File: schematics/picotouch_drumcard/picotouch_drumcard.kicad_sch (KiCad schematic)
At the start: 77 parts, among them J1 AudioJack4, J2 AudioJack4, J3 AudioJack4, SW1 Capacitive Button, SW10 Capacitive Button, SW11 Capacitive Button, SW12 Capacitive Button, SW13 Capacitive Button, SW14 Capacitive Button, SW15 Capacitive Button, SW16 Capacitive Button, SW17 Capacitive Button, SW2 Capacitive Button, SW3 Capacitive Button, SW4 Capacitive Button, SW5 Capacitive Button, SW6 Capacitive Button, SW7 Capacitive Button, SW8 Capacitive Button, SW9 Capacitive Button, U1 Pico, U2 H11L1S(TA), U3 MCP73831-2-OT, U4 TS20, X1 AFC20-S02ACA-00

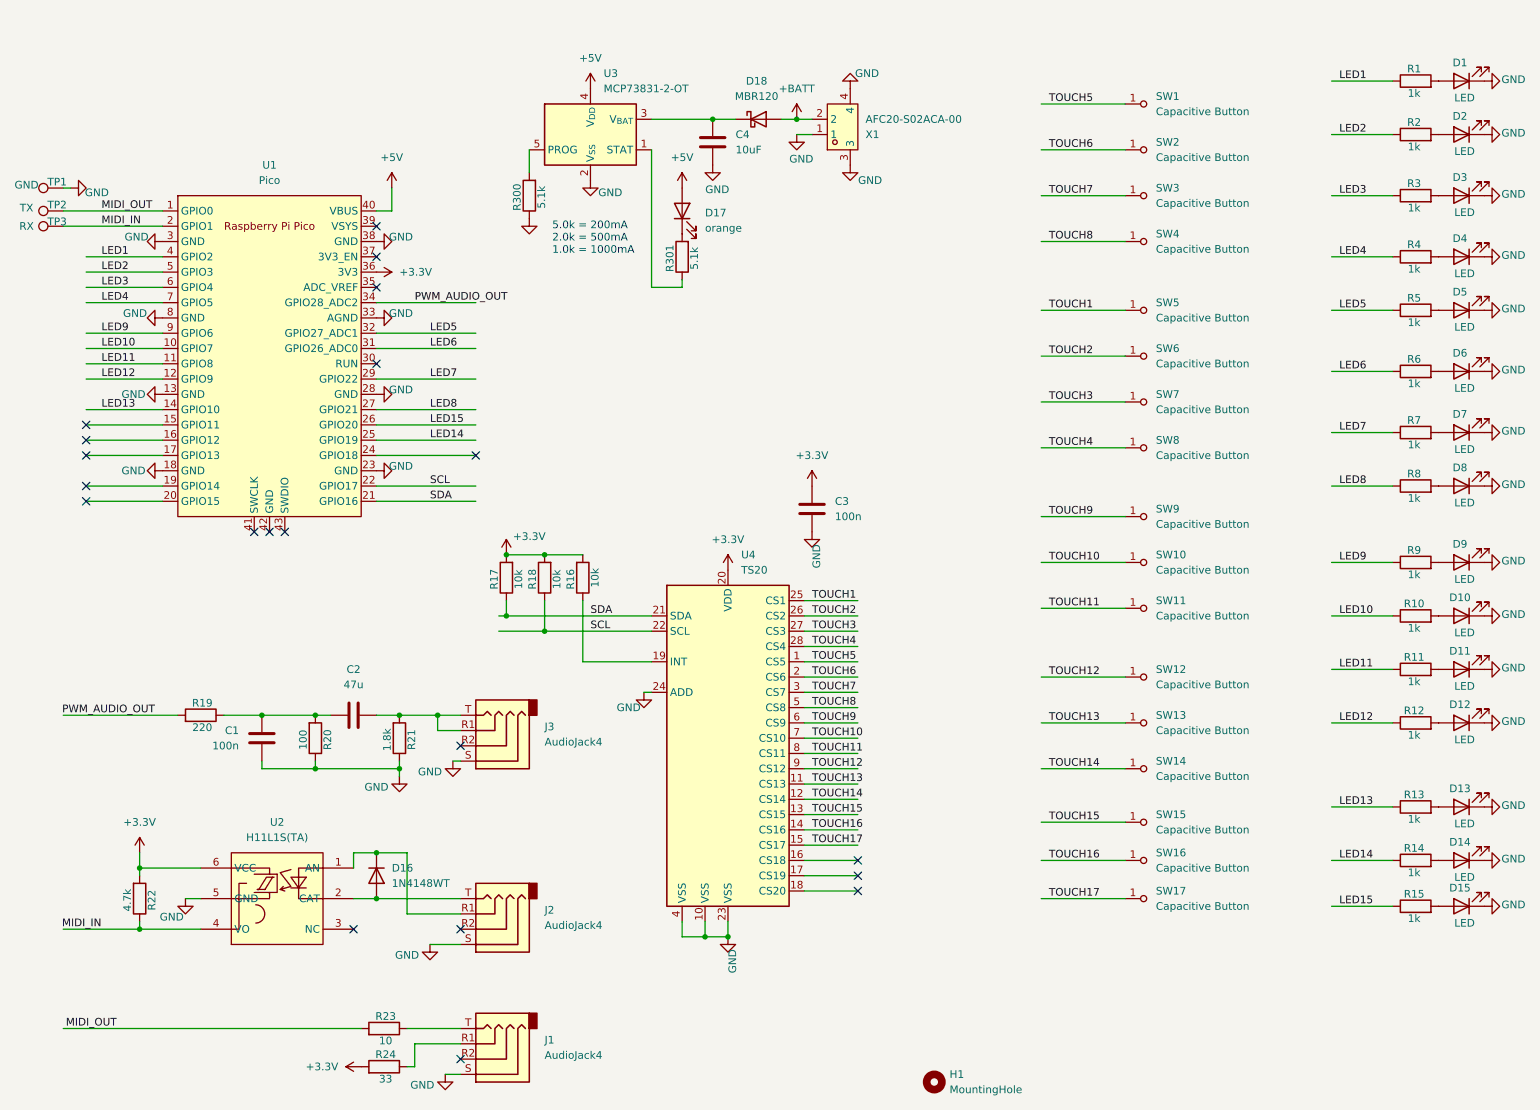
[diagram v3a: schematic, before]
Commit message: add missing cap on opto
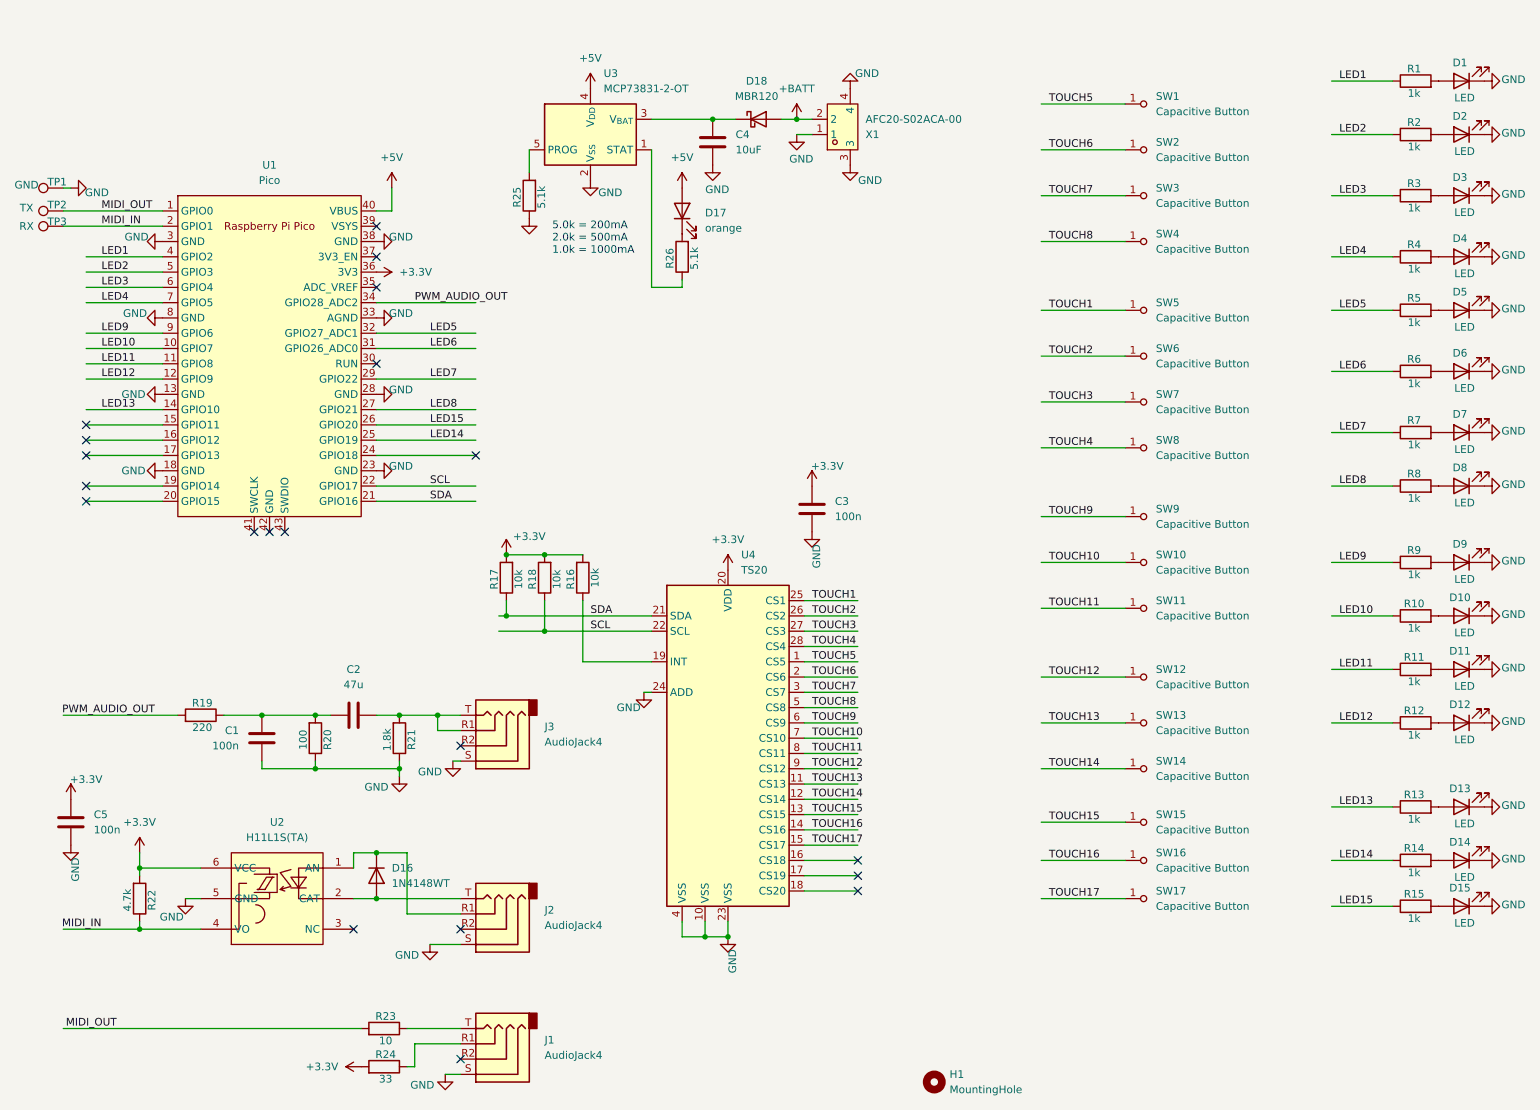
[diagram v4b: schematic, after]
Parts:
- added C5: 100n, Capacitor_SMD:C_0603_1608Metric, symbol Device:C
- renumbered R300 to R25, R301 to R26
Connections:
- net +3.3V: now also C5.1
- net GND: now also C5.2
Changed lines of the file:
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@@
 		(on_board yes)
 		(dnp no)
-		(property "Reference" "R301"
+		(property "Reference" "R26"
 			(at 126.238 53.594 90)
 			(effects
@@
 			(project "picotouch_drumcard"
 				(path "/5e315703-690d-40b0-a846-b905406b612c"
-					(reference "R301")
+					(reference "R26")
 					(unit 1)
 				)
@@
 	)
 	(symbol
+		(lib_id "Device:C")
+		(at 26.67 147.32 0)
+		(unit 1)
+		(exclude_from_sim no)
+		(in_bom yes)
+		(on_board yes)
+		(dnp no)
+		(fields_autoplaced yes)
+		(property "Reference" "C5"
+			(at 30.48 146.0499 0)
+			(effects
+				(font
+					(size 1.27 1.27)
+				)
+				(justify left)
+			)
+		)
+		(property "Value" "100n"
+			(at 30.48 148.5899 0)
+			(effects
+				(font
+					(size 1.27 1.27)
+				)
+				(justify left)
+			)
+		)
+		(property "Footprint" "Capacitor_SMD:C_0603_1608Metric"
+			(at 27.6352 151.13 0)
+			(effects
+				(font
+					(size 1.27 1.27)
+				)
+				(hide yes)
+			)
+		)
+		(property "Datasheet" "~"
+			(at 26.67 147.32 0)
+			(effects
+				(font
+					(size 1.27 1.27)
+				)
+				(hide yes)
+			)
+		)
+		(property "Description" "Unpolarized capacitor"
+			(at 26.67 147.32 0)
+			(effects
+				(font
+					(size 1.27 1.27)
+				)
+				(hide yes)
+			)
+		)
+		(pin "2"
+		)
+		(pin "1"
+		)
+		(instances
+			(project "picotouch_drumcard"
+				(path "/5e315703-690d-40b0-a846-b905406b612c"
+					(reference "C5")
+					(unit 1)
+				)
+			)
+		)
+	)
+	(symbol
 		(lib_id "power:GND")
 		(at 261.62 121.92 90)
@@
 		(on_board yes)
 		(dnp no)
-		(fields_autoplaced yes)
 		(property "Reference" "#PWR027"
 			(at 149.86 95.25 0)
@@
 		)
 		(property "Value" "+3.3V"
-			(at 149.86 86.36 0)
+			(at 152.4 88.138 0)
 			(effects
 				(font
@@
 		(on_board yes)
 		(dnp no)
-		(property "Reference" "R300"
+		(property "Reference" "R25"
 			(at 100.838 43.434 90)
 			(effects
@@
 			(project "picotouch_drumcard"
 				(path "/5e315703-690d-40b0-a846-b905406b612c"
-					(reference "R300")
+					(reference "R25")
 					(unit 1)
 				)
@@
 	)
 	(symbol
+		(lib_id "power:+3.3V")
+		(at 26.67 143.51 0)
+		(unit 1)
+		(exclude_from_sim no)
+		(in_bom yes)
+		(on_board yes)
+		(dnp no)
+		(property "Reference" "#PWR049"
+			(at 26.67 147.32 0)
+			(effects
+				(font
+					(size 1.27 1.27)
+				)
+				(hide yes)
+			)
+		)
+		(property "Value" "+3.3V"
+			(at 29.21 140.208 0)
+			(effects
+				(font
+					(size 1.27 1.27)
+				)
+			)
+		)
+		(property "Footprint" ""
+			(at 26.67 143.51 0)
+			(effects
+				(font
+					(size 1.27 1.27)
+				)
+				(hide yes)
+			)
+		)
+		(property "Datasheet" ""
+			(at 26.67 143.51 0)
+			(effects
+				(font
+					(size 1.27 1.27)
+				)
+				(hide yes)
+			)
+		)
+		(property "Description" "Power symbol creates a global label with name \"+3.3V\""
+			(at 26.67 143.51 0)
+			(effects
+				(font
+					(size 1.27 1.27)
+				)
+				(hide yes)
+			)
+		)
+		(pin "1"
+		)
+		(instances
+			(project "picotouch_drumcard"
+				(path "/5e315703-690d-40b0-a846-b905406b612c"
+					(reference "#PWR049")
+					(unit 1)
+				)
+			)
+		)
+	)
+	(symbol
 		(lib_id "SparkFun-Switch:Capacitive Button")
 		(at 201.93 27.94 270)
@@
 					(unit 1)
 				)
+			)
+		)
+	)
+	(symbol
+		(lib_id "power:GND")
+		(at 26.67 151.13 0)
+		(unit 1)
+		(exclude_from_sim no)
+		(in_bom yes)
+		(on_board yes)
+		(dnp no)
+		(property "Reference" "#PWR050"
+			(at 26.67 157.48 0)
+			(effects
+				(font
+					(size 1.27 1.27)
+				)
+				(hide yes)
+			)
+		)
+		(property "Value" "GND"
+			(at 27.432 155.194 90)
+			(effects
+				(font
+					(size 1.27 1.27)
+				)
+			)
+		)
+		(property "Footprint" ""
+			(at 26.67 151.13 0)
+			(effects
+				(font
+					(size 1.27 1.27)
+				)
+				(hide yes)
+			)
+		)
+		(property "Datasheet" ""
+			(at 26.67 151.13 0)
+			(effects
+				(font
+					(size 1.27 1.27)
+				)
+				(hide yes)
+			)
+		)
+		(property "Description" "Power symbol creates a global label with name \"GND\" , ground"
+			(at 26.67 151.13 0)
+			(effects
+				(font
+					(size 1.27 1.27)
+				)
+				(hide yes)
+			)
+		)
+		(pin "1"
+		)
+		(instances
+			(project "picotouch_drumcard"
+				(path "/5e315703-690d-40b0-a846-b905406b612c"
+					(reference "#PWR050")
+					(unit 1)
+				)

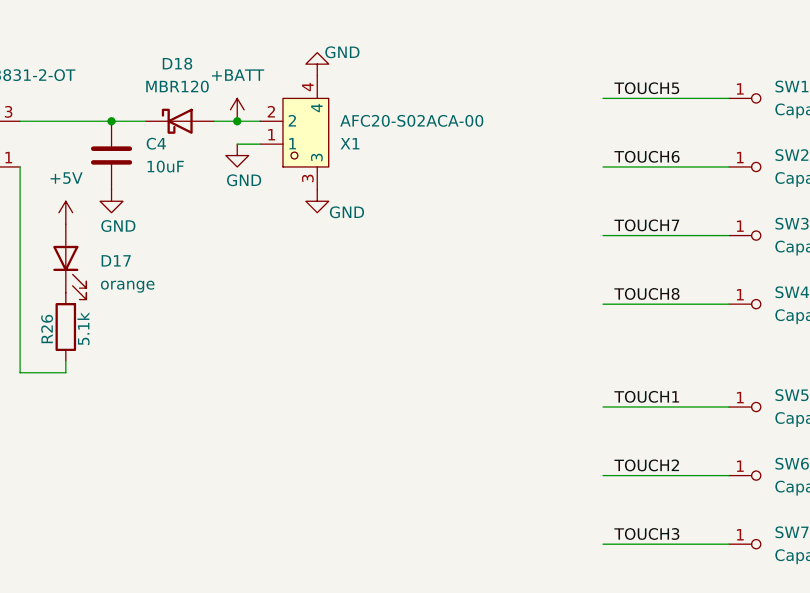
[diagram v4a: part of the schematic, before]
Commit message: dangit forgot power switch
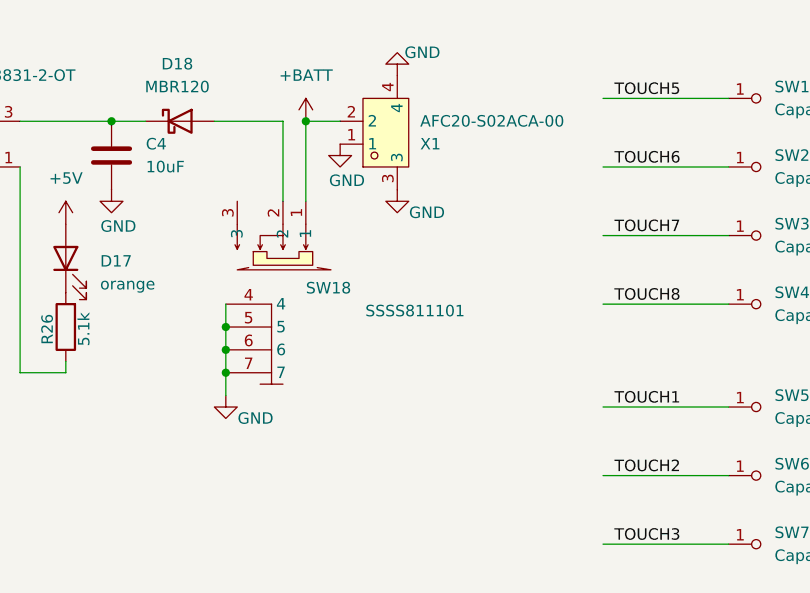
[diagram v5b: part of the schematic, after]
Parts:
- added SW18: SSSS811101, easyeda2kicad:SW-SMD_SSSS811101, symbol easyeda2kicad:SSSS811101
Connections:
- net +BATT: now also SW18.1; no longer D18.2 (A)
- net GND: now also SW18.4, SW18.5, SW18.6, SW18.7
- new net: D18.2 (A), SW18.2
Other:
- moved on the sheet: X1

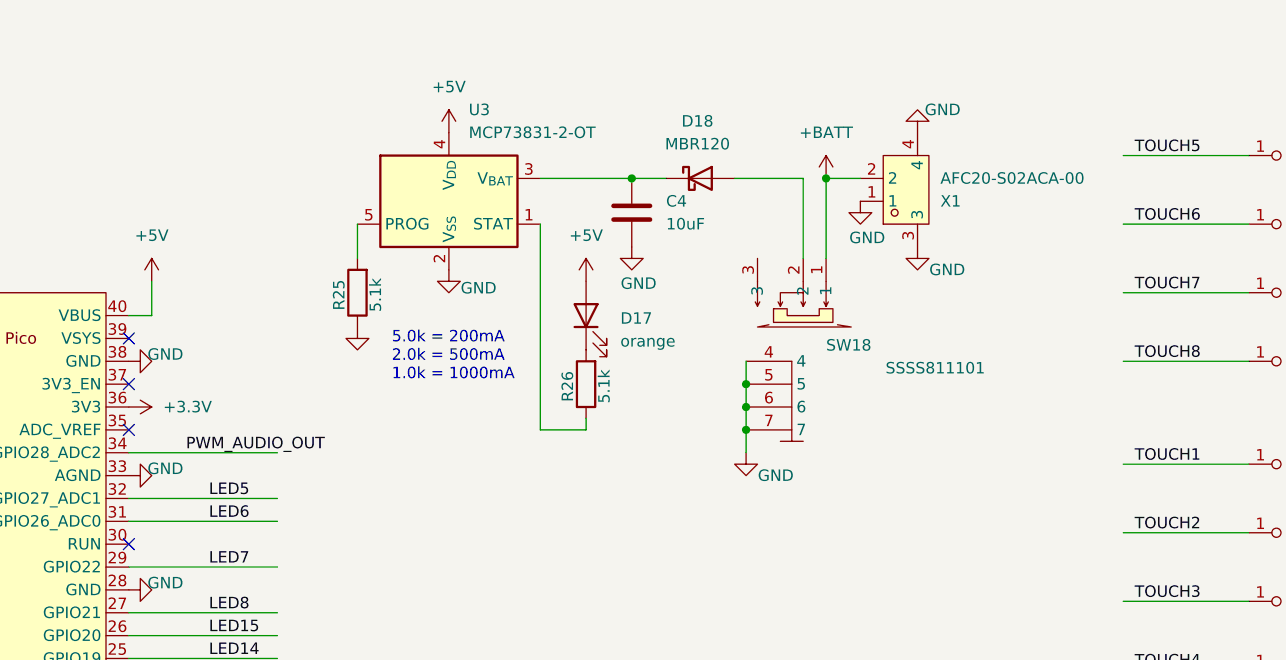
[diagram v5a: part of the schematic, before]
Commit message: add missing cap to charger circuit, nudge around charger to fit
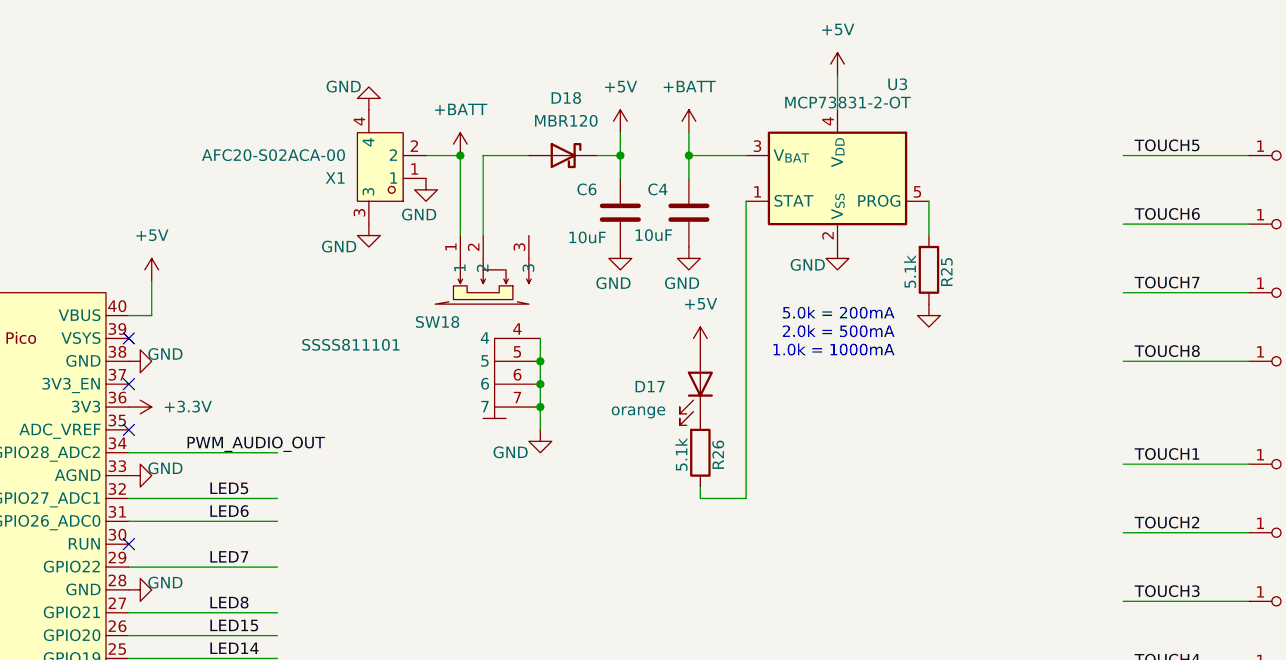
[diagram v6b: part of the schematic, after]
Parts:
- added C6: 10uF, Capacitor_SMD:C_0603_1608Metric, symbol Device:C
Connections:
- net +5V: now also D18.1 (K), C6.1
- net +BATT: now also C4.1, U3.3 (V_{BAT})
- net GND: now also C6.2
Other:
- moved on the sheet: C4, D17, D18, R25, R26, SW18, U3, X1
